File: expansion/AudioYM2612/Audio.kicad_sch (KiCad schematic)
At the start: 40 parts, among them U3 YM2612, U4 SN76489, U5 LTC6903, U6 LTC6903, U7 TL062

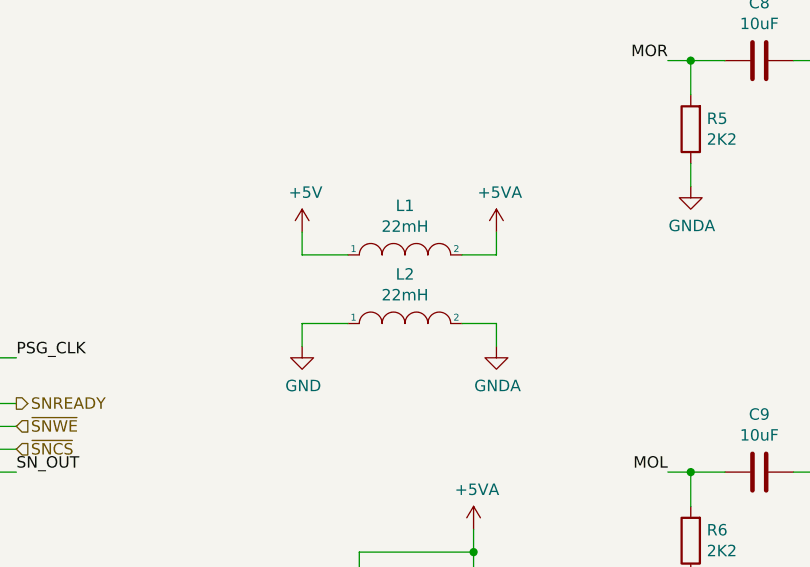
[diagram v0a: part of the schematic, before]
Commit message: All projects updated to KiCAD 7 format files
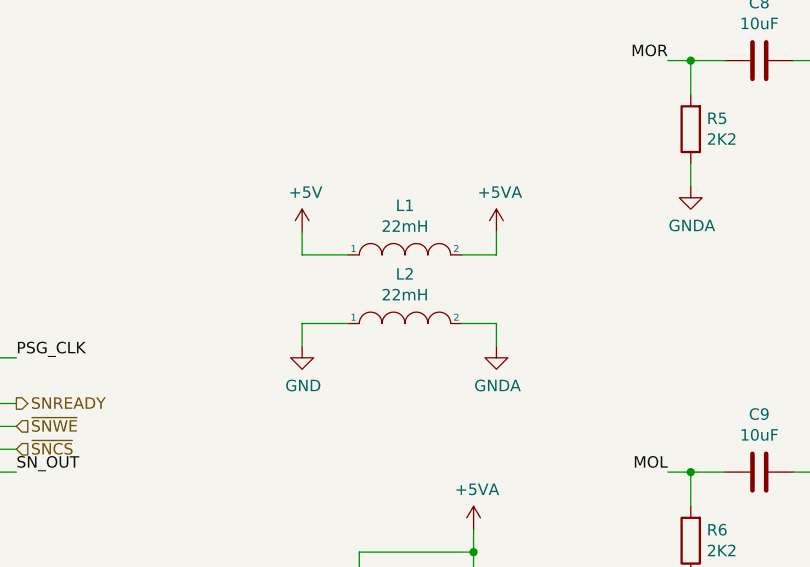
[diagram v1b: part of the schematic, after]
